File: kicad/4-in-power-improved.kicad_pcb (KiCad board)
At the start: 4 copper layers, 84.1 x 61.7 mm, 200 parts, among them J1 USB_C_Receptacle_USB2.0_16P, J2 Bus_PCI_Express_x1, Q1 FMMT493, Q2 AO3400A, Q3 AO3400A, U1 XC6206P332MR, U10 BQ25672RQMR, U11 TPS54331DR, U12 6.8uH, U13 TPS54331DR, U14 6.8uH, U15 LM5157RTER, U17 2P SMD 2.54P Jumper, U2 2P SMD 2.54P Jumper, U3 W25Q128JVP, U4 2P SMD 2.54P Jumper, U5 MCP25625T-E/ML, U6 RP2040, U7 S5B-XH-A(LF)(SN), U8 XT30PW-M, U9 BQ7694202PFBR, X1 ABM8-272-T3, Y1 X322516MLB4SI

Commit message: Silk screen UI changes
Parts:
- added D17: Yellow, PCM_JLCPCB:D_0603, F.Cu at (174.7, 103.8)
- added G***: LOGO, LOGO, F.Cu at (157.6, 119.4)
- added R57: 10kΩ, PCM_JLCPCB:R_0402, F.Cu at (173.5, 104.4)
- added REF**: AMASS_XT30U-F_1x02_P5.0mm_Vertical, 4in-power:AMASS_XT30U-F_1x02_P5.0mm_Vertical, F.Cu at (133.5, 116.3)
- added TP20: RH-5015, 4in-power:SMD_RH-5015, B.Cu at (163.9, 89.3)
- added TP21: RH-5015, 4in-power:SMD_RH-5015, B.Cu at (166.2, 92.0)
- added TP22: RH-5015, 4in-power:SMD_RH-5015, B.Cu at (174.3, 73.5)
- added TP23: RH-5015, 4in-power:SMD_RH-5015, B.Cu at (159.0, 91.7)
- added TP24: RH-5015, 4in-power:SMD_RH-5015, B.Cu at (174.0, 70.1)
- J2: footprint Connector_PCBEdge:BUS_PCIexpress_x1 -> 4in-power:BUS_PCIexpress_x1
- REF** (x2): footprint Connector_AMASS:AMASS_XT30U-F_1x02_P5.0mm_Vertical -> 4in-power:AMASS_XT30U-F_1x02_P5.0mm_Vertical
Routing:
- net +24V: track 11.0 -> 63.8 mm, vias 0 -> 2
- net +3.3V: track 84.4 -> 78.7 mm
- net Net-(U8-+): track 7.73 -> 13.4 mm
- net VSS: track 43.1 -> 48.8 mm
- net +5V: track 35.6 -> 39.3 mm
- net /Power/StepDown3.3V/SW: track 5.30 -> 2.50 mm
- net GND: track 136.5 -> 138.3 mm, vias 114 -> 116
- net /CANN: track 59.5 -> 57.8 mm
- net Net-(D17-Pad2): track 0.00 -> 1.33 mm
- net /CANP: track 59.8 -> 58.6 mm
- net /SCL1: track 54.3 -> 54.9 mm
- net /QSPI_SS: track 15.0 -> 15.5 mm
- net /EN_5V: track 38.5 -> 38.0 mm
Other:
- board text added: "+"
- board text added: "+24V"
- board text added: "+3.3V"
- board text added: "+5V"
- board text added: "-"
- board text added: "3.3V SW"
- board text added: "3.6V-24V MAX"
- board text added: "5V SW"
- board text added: "BAT+"
- board text added: "BAT-"
- board text added: "BMS"
- board text added: "BMS TRANS E"
- board text added: "CELL1"
- board text added: "CELL2"
- board text added: "CELL3"
- board text added: "CHARGER"
- board text added: "CHG FET G"
- board text added: "CHG REG"
- board text added: "CHG SW1"
- board text added: "CHG SW2"
- board text added: "DSG FET G"
- board text added: "GND"
- board text added: "PACK+"
- board text added: "ROUND IS GROUND"
- board text added: "RST"
- board text added: "Radio Jammer -TS"
- board text added: "SWD"
- board text added: "VIN"
- board text added: "VIN: 13.2V MIN 16.2V MAX"
- board text added: "VSS"
- board text added: "VSYS"

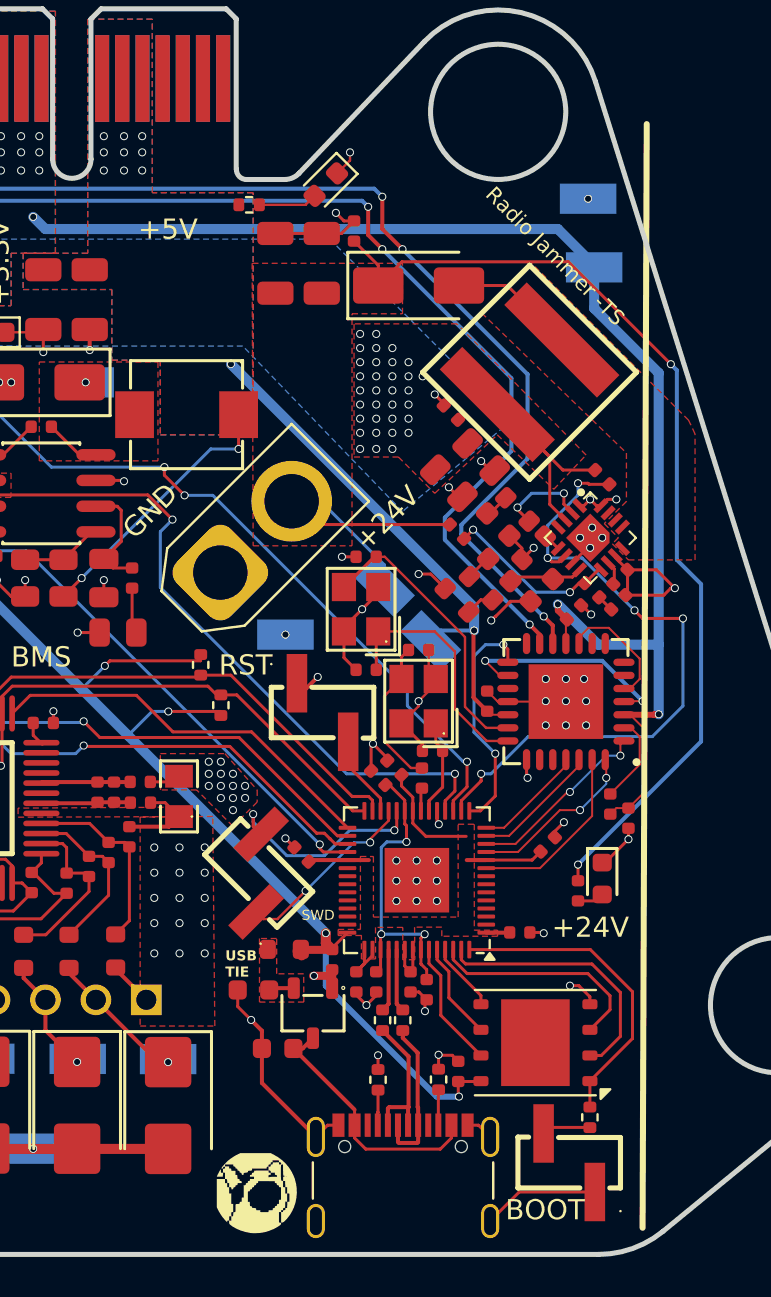
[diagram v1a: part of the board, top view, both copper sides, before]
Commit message: Replace R26 with R1206 footprint and update PCB
Replaced the R26 resistor from an R0805 to an R1206 footprint in the PCB layout and netlist, updated associated tracks and vias, and added the new R1206 footprint file. Updated schematic, BOM, designators, and positions to reflect this change. Cleaned up related net connections and removed the old R0805 instance.
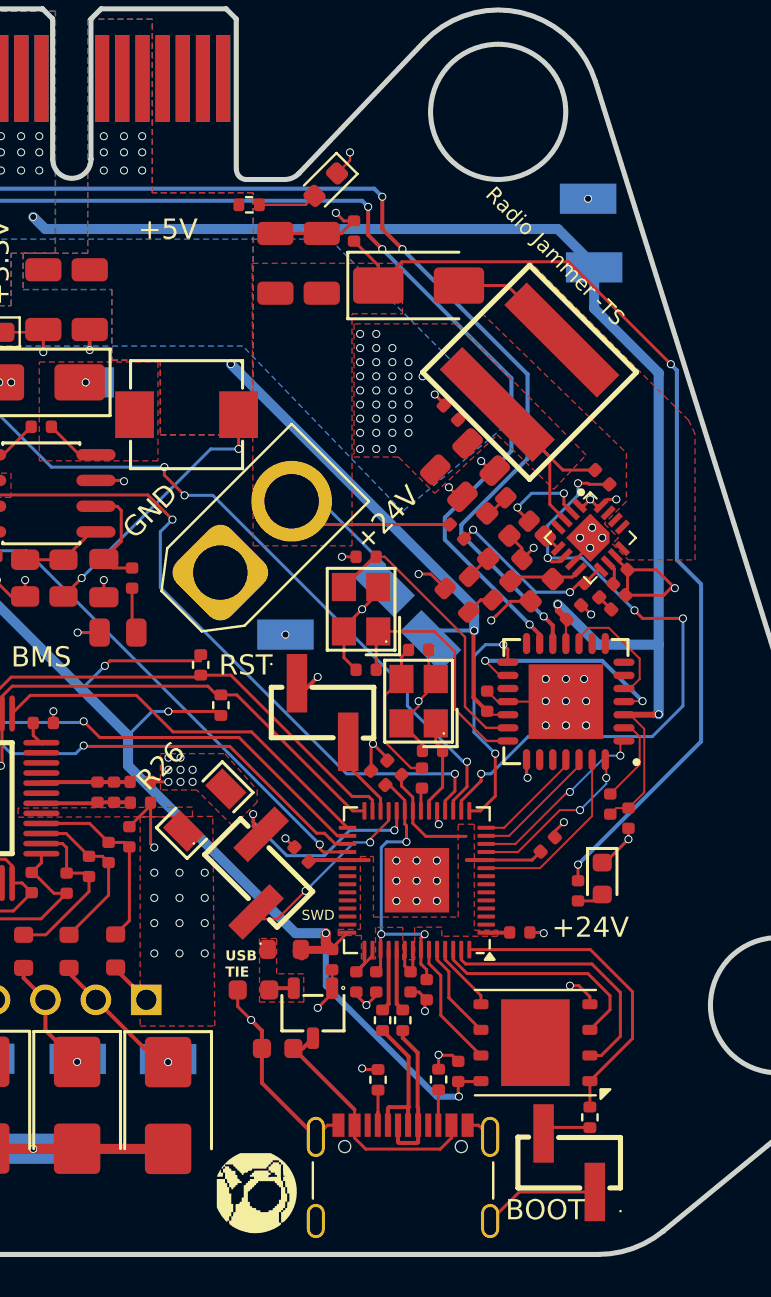
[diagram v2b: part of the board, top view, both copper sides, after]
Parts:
- R26: value 5mΩ -> PMR18EZPFV2L00; footprint 4in-power:R0805 -> 4in-power:R1206
- moved R26 1.45 mm to (155.0, 100.4), turned to 45 degrees
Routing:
- net /MCU_REG: track 82.0 -> 82.9 mm
- net VSS: track 48.8 -> 48.3 mm, vias 23 -> 21
- net GND: track 138.3 -> 138.1 mm, vias 116 -> 111
